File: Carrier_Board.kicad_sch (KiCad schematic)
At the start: 6 parts

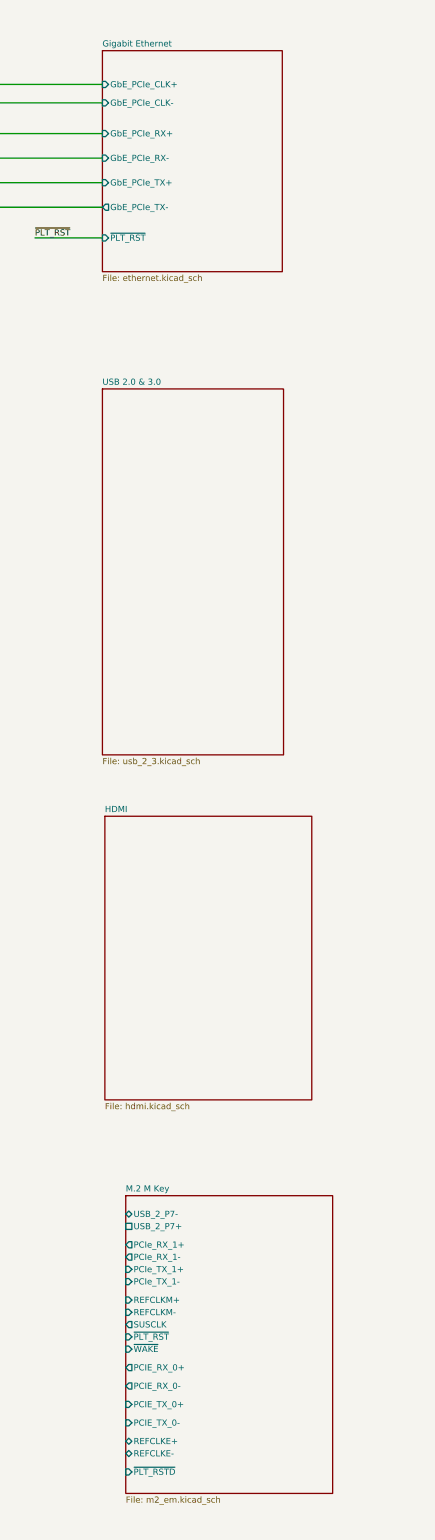
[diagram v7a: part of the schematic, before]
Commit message: Finished the schematic capture for the USb 2.0/3.0
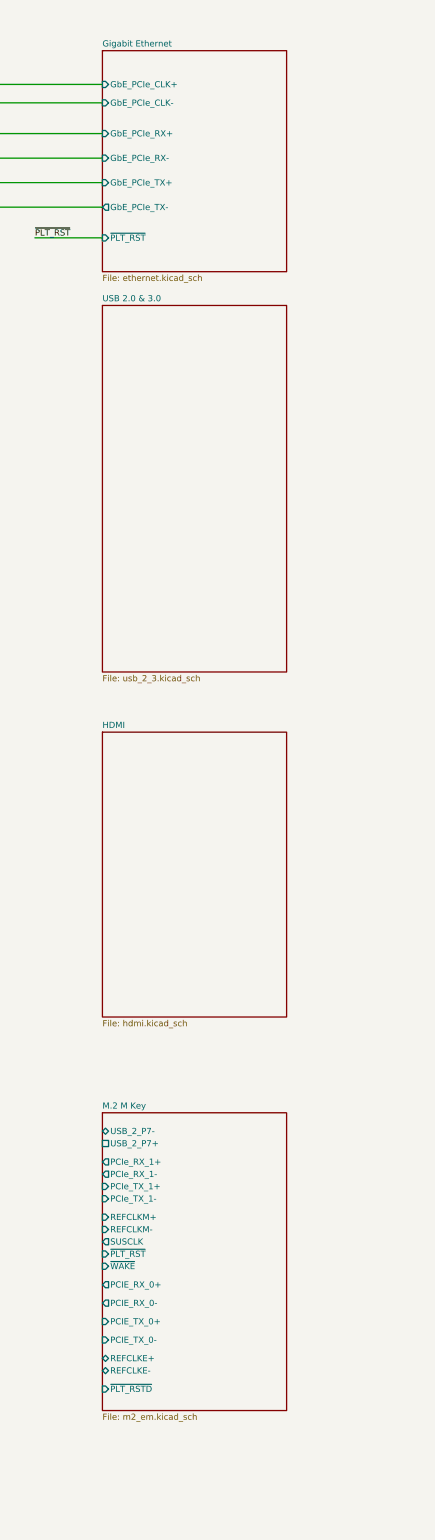
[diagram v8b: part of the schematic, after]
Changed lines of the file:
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@@
 	)
 	(sheet
-		(at 325.628 240.284)
-		(size 42.799 58.674)
+		(at 325.12 222.885)
+		(size 38.1 58.928)
 		(exclude_from_sim no)
 		(in_bom yes)
@@
 		)
 		(property "Sheetname" "HDMI"
-			(at 325.628 239.5724 0)
+			(at 325.12 222.1734 0)
 			(show_name no)
 			(do_not_autoplace no)
@@
 		)
 		(property "Sheetfile" "hdmi.kicad_sch"
-			(at 325.628 299.5426 0)
+			(at 325.12 282.3976 0)
 			(show_name no)
 			(do_not_autoplace no)
@@
 	(sheet
 		(at 325.12 81.915)
-		(size 37.211 45.72)
+		(size 38.1 45.72)
 		(exclude_from_sim no)
 		(in_bom yes)
@@
 	)
 	(sheet
-		(at 329.946 318.77)
-		(size 42.799 61.595)
+		(at 325.12 301.625)
+		(size 38.1 61.595)
 		(exclude_from_sim no)
 		(in_bom yes)
@@
 		)
 		(property "Sheetname" "M.2 M Key"
-			(at 329.946 318.0584 0)
+			(at 325.12 300.9134 0)
 			(show_name no)
 			(do_not_autoplace no)
@@
 		)
 		(property "Sheetfile" "m2_em.kicad_sch"
-			(at 329.946 380.9496 0)
+			(at 325.12 363.8046 0)
 			(show_name no)
 			(do_not_autoplace no)
@@
 		)
 		(pin "PCIe_RX_1+" output
-			(at 329.946 328.93 180)
+			(at 325.12 311.785 180)
 			(effects
 				(font
@@
 		)
 		(pin "PCIe_RX_1-" output
-			(at 329.946 331.47 180)
+			(at 325.12 314.325 180)
 			(effects
 				(font
@@
 		)
 		(pin "PCIe_TX_1+" input
-			(at 329.946 334.01 180)
+			(at 325.12 316.865 180)
 			(effects
 				(font
@@
 		)
 		(pin "PCIe_TX_1-" input
-			(at 329.946 336.55 180)
+			(at 325.12 319.405 180)
 			(effects
 				(font
@@
 		)
 		(pin "REFCLKM+" input
-			(at 329.946 340.36 180)
+			(at 325.12 323.215 180)
 			(effects
 				(font
@@
 		)
 		(pin "REFCLKM-" input
-			(at 329.946 342.9 180)
+			(at 325.12 325.755 180)
 			(effects
 				(font
@@
 		)
 		(pin "SUSCLK" output
-			(at 329.946 345.44 180)
+			(at 325.12 328.295 180)
 			(effects
 				(font
@@
 		)
 		(pin "~{PLT_RST}" input
-			(at 329.946 347.98 180)
+			(at 325.12 330.835 180)
 			(effects
 				(font
@@
 		)
 		(pin "~{WAKE}" input
-			(at 329.946 350.52 180)
+			(at 325.12 333.375 180)
 			(effects
 				(font
@@
 		)
 		(pin "PCIE_RX_0+" output
-			(at 329.946 354.33 180)
+			(at 325.12 337.185 180)
 			(effects
 				(font
@@
 		)
 		(pin "PCIE_RX_0-" output
-			(at 329.946 358.14 180)
+			(at 325.12 340.995 180)
 			(effects
 				(font
@@
 		)
 		(pin "PCIE_TX_0+" input
-			(at 329.946 361.95 180)
+			(at 325.12 344.805 180)
 			(effects
 				(font
@@
 		)
 		(pin "PCIE_TX_0-" input
-			(at 329.946 365.76 180)
+			(at 325.12 348.615 180)
 			(effects
 				(font
@@
 		)
 		(pin "REFCLKE+" bidirectional
-			(at 329.946 369.57 180)
+			(at 325.12 352.425 180)
 			(effects
 				(font
@@
 		)
 		(pin "REFCLKE-" bidirectional
-			(at 329.946 372.11 180)
+			(at 325.12 354.965 180)
 			(effects
 				(font
@@
 		)
 		(pin "USB_2_P7+" passive
-			(at 329.946 325.12 180)
+			(at 325.12 307.975 180)
 			(effects
 				(font
@@
 		)
 		(pin "USB_2_P7-" bidirectional
-			(at 329.946 322.58 180)
+			(at 325.12 305.435 180)
 			(effects
 				(font
@@
 		)
 		(pin "~{PLT_RSTD}" input
-			(at 329.946 375.92 180)
+			(at 325.12 358.775 180)
 			(effects
 				(font
@@
 	)
 	(sheet
-		(at 325.12 151.892)
-		(size 37.465 75.692)
+		(at 325.12 134.62)
+		(size 38.1 75.819)
 		(exclude_from_sim no)
 		(in_bom yes)
@@
 		)
 		(property "Sheetname" "USB 2.0 & 3.0"
-			(at 325.12 151.1804 0)
+			(at 325.12 133.9084 0)
 			(show_name no)
 			(do_not_autoplace no)
@@
 		)
 		(property "Sheetfile" "usb_2_3.kicad_sch"
-			(at 325.12 228.1686 0)
+			(at 325.12 211.0236 0)
 			(show_name no)
 			(do_not_autoplace no)
